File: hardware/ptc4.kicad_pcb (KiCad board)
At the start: 4 copper layers, 100 x 85 mm, 128 parts, among them J101 TNG-Power-TOP, J102 TNG-Power-BTM, J103 TNG-Data-TOP, J104 TNG-Data-BTM, P102 Debug, P103 PE, P201 INPUT0, P202 INPUT1, P203 INPUT2, P204 INPUT3, SW101 BOOT, U101 STM32F070CBT6, U102 AZ1117EH, U103 82400152, U104 TPS22975, U105 PDME1-S5-S5-S, U201 MAX31865, U202 MAX31865, U203 MAX31865, U204 MAX31865, U205 ISO7741DWR, U206 ISO7741DWR, U207 AZ1117EH, X101 TBD

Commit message: rename
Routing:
- net Net-(C120-Pad1): track 23.1 -> 34.7 mm
- net A5V: track 14.8 -> 21.6 mm
- net AGND: track 53.9 -> 60.6 mm
- net Net-(C121-Pad1): track 12.3 -> 18.4 mm
- net GND: track 170.8 -> 176.0 mm

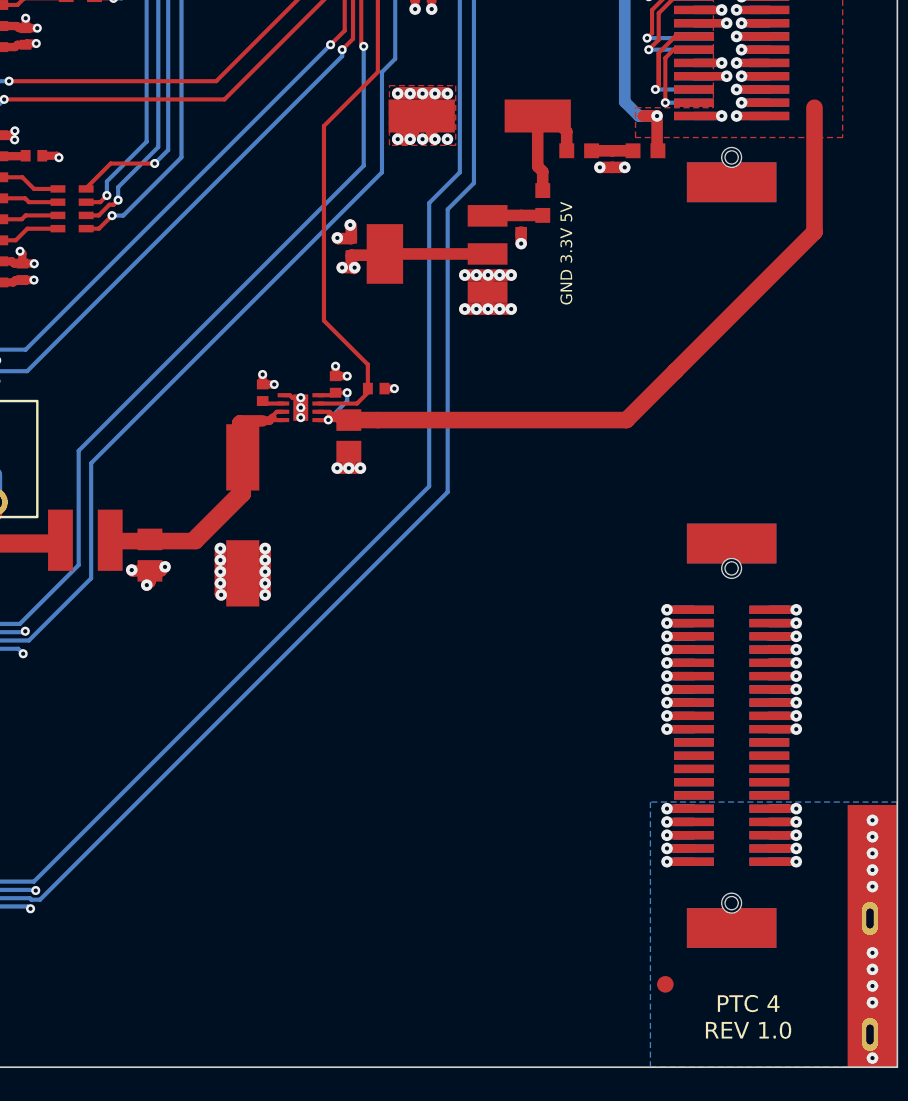
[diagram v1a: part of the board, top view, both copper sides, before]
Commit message: add version 1.1
fix footprints
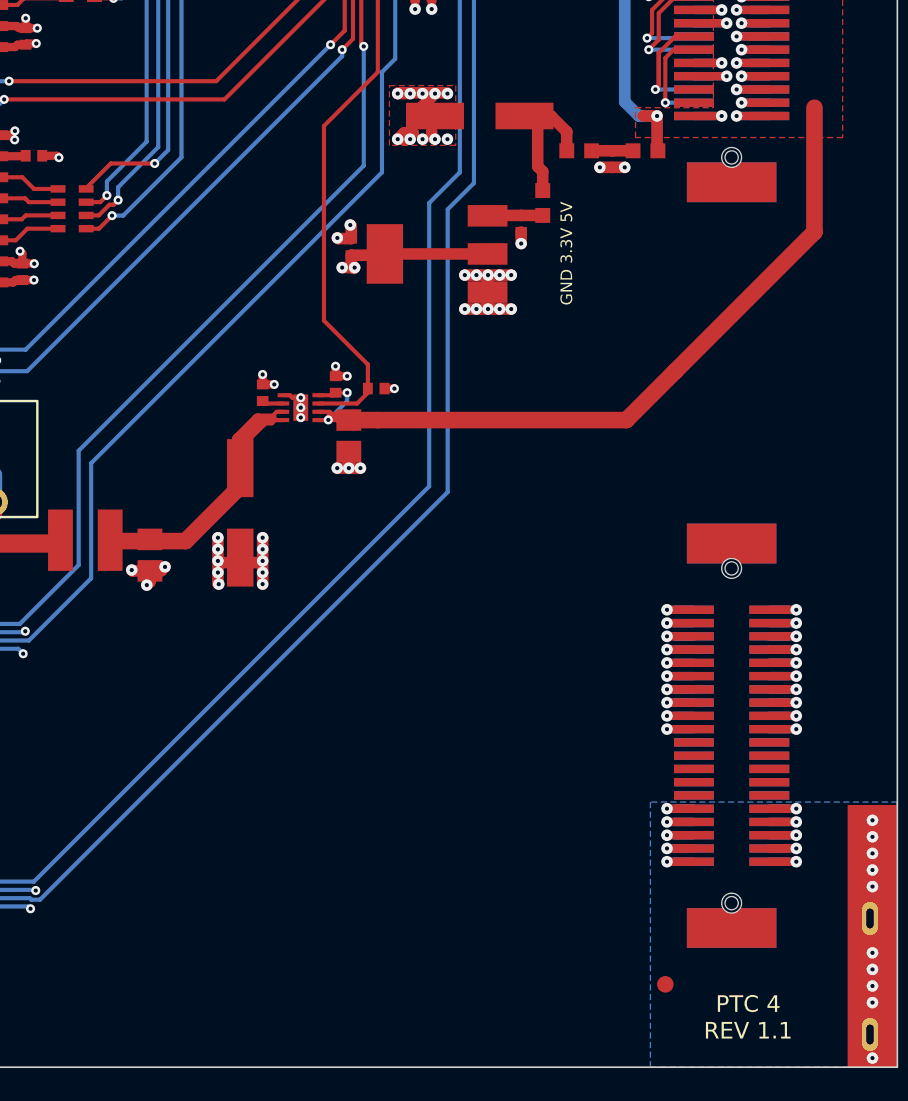
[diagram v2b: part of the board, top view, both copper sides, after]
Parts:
- C108, C109: value TBD -> 12pF
- C111, C120: value TBD -> 100µF; footprint kicad-libraries:ELKO_83 -> kicad-libraries:ELKO_63
- X101: value TBD -> 8MHz
- moved C120 0.21 mm to (150.2, 114.0)
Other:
- board text added: "Copyright Tinkerforge GmbH 2020. This documentation describes Open Hardware and is licensed under the CERN OHL v. 1.1. You may redistribute and modify this documentation under the terms of the CERN OHL v.1.1. (http://ohwr.org/cernohl). This documentation is distributed WITHOUT ANY EXPRESS OR IMPLIED WARRANTY, INCLUDING OF MERCHANTABILITY, SATISFACTORY QUALITY AND FITNESS FOR A PARTICULAR PURPOSE.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"
- board text added: "PTC 4 REV 1.1"
- board text removed: "PTC 4 REV 1.0"

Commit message: fix values
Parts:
- C108, C109: value 12pF -> 33pF
- C113, C114: value TBD/47pF -> 47pF

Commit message: fix footprint
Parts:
- C110: footprint C0805 -> kicad-libraries:C0805E

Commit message: fix values
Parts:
- C111, C120: value 100µF -> 100uF
- C121, C122, C123, C126: value 4.7µF/16V -> 4.7uF/16V
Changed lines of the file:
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@@
       (effects (font (size 0.2 0.2) (thickness 0.05)))
     )
-    (fp_text value 4.7µF/16V (at 0 -0.4) (layer F.Fab)
+    (fp_text value 4.7uF/16V (at 0 -0.4) (layer F.Fab)
       (effects (font (size 0.2 0.2) (thickness 0.05)))
     )
@@
       (effects (font (size 0.2 0.2) (thickness 0.05)))
     )
-    (fp_text value 4.7µF/16V (at 0 -0.4) (layer F.Fab)
+    (fp_text value 4.7uF/16V (at 0 -0.4) (layer F.Fab)
       (effects (font (size 0.2 0.2) (thickness 0.05)))
     )
@@
       (effects (font (size 0.2 0.2) (thickness 0.05)))
     )
-    (fp_text value 4.7µF/16V (at 0 -0.4 90) (layer F.Fab)
+    (fp_text value 4.7uF/16V (at 0 -0.4 90) (layer F.Fab)
       (effects (font (size 0.2 0.2) (thickness 0.05)))
     )
@@
       (effects (font (size 0.2 0.2) (thickness 0.05)))
     )
-    (fp_text value 4.7µF/16V (at 0 -0.4 90) (layer F.Fab)
+    (fp_text value 4.7uF/16V (at 0 -0.4 90) (layer F.Fab)
       (effects (font (size 0.2 0.2) (thickness 0.05)))
     )
@@
       (effects (font (size 0.59944 0.59944) (thickness 0.12446)))
     )
-    (fp_text value 100µF (at 0.95 -0.375) (layer F.Fab)
+    (fp_text value 100uF (at 0.95 -0.375) (layer F.Fab)
       (effects (font (size 0.59944 0.59944) (thickness 0.12446)))
     )
@@
       (effects (font (size 0.59944 0.59944) (thickness 0.12446)))
     )
-    (fp_text value 100µF (at 0.95 -0.375 90) (layer F.Fab)
+    (fp_text value 100uF (at 0.95 -0.375 90) (layer F.Fab)
       (effects (font (size 0.59944 0.59944) (thickness 0.12446)))
     )

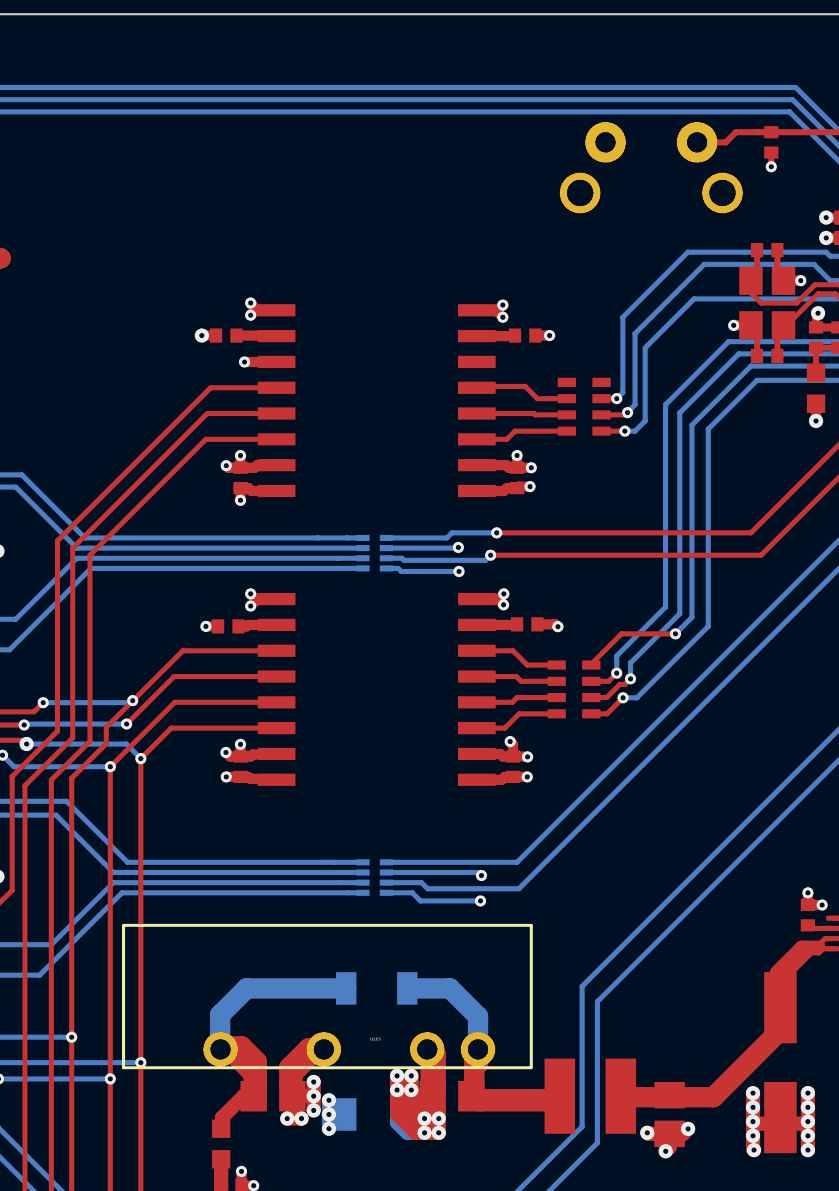
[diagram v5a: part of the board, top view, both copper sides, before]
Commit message: all footprints updated
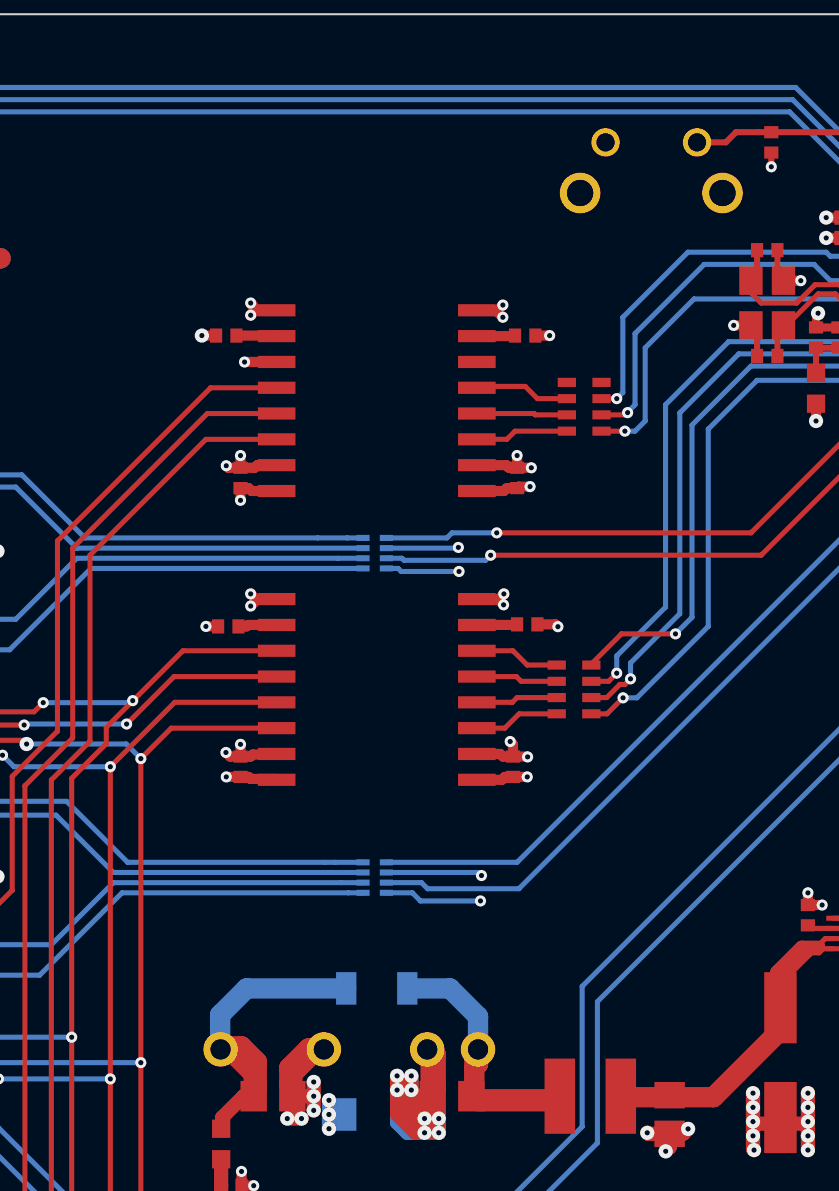
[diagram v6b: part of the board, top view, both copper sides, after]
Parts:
- C101, C102, C103, C104, C105, C106, C107, C108, C109, C112, C113, C114, C116, C117, C118, C119, C201, C202, C203, C204, C205, C206, C207, C208, C209, C210, C211, C212, C213, C214, C215, C216, C217, C218, C219: footprint C0402F -> kicad-libraries:C0402F
- C115: footprint C0603F -> kicad-libraries:C0603F
- D203, D204, D205, D206, D207, D208, D209, D210: footprint LED-LP -> kicad-libraries:LED-LP
- J101, J103: footprint TNG-40-TOP -> kicad-libraries:TNG-40-TOP
- J102, J104: footprint TNG-40-BTM -> kicad-libraries:TNG-40-BTM
- L101, L102, L103, L104, L209: footprint R0603F -> kicad-libraries:R0603F
- L105: footprint WE-CNSW-0603 -> kicad-libraries:WE-CNSW-0603
- LED101: footprint LED-RGB-LP -> kicad-libraries:LED-RGB-LP
- P201, P202, P203, P204: footprint OQ_4P -> kicad-libraries:OQ_4P
- R101, R102, R103, R104, R105, R106, R107, R108, R109: footprint R0402F -> kicad-libraries:R0402F
- U103: footprint SOT563-SPEC -> kicad-libraries:SOT563-SPEC

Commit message: default is non isolated
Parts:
- C101, C102, C103, C104, C105, C106, C107, C108, C109, C112, C113, C114, C116, C117, C118, C119, C201, C202, C203, C204, C205, C206, C207, C208, C209, C210, C211, C212, C213, C214, C215, C216, C217, C218, C219: footprint kicad-libraries:C0402F -> C0402F
- C115: footprint kicad-libraries:C0603F -> C0603F
- D203, D204, D205, D206, D207, D208, D209, D210: footprint kicad-libraries:LED-LP -> LED-LP
- J101, J103: footprint kicad-libraries:TNG-40-TOP -> TNG-40-TOP
- J102, J104: footprint kicad-libraries:TNG-40-BTM -> TNG-40-BTM
- L101, L102, L103, L104, L209: footprint kicad-libraries:R0603F -> R0603F
- L105: footprint kicad-libraries:WE-CNSW-0603 -> WE-CNSW-0603
- LED101: footprint kicad-libraries:LED-RGB-LP -> LED-RGB-LP
- P201, P202, P203, P204: footprint kicad-libraries:OQ_4P -> OQ_4P
- R101, R102, R103, R104, R105, R106, R107, R108, R109: footprint kicad-libraries:R0402F -> R0402F
- R110, R111: value DNP -> 0
- U103: footprint kicad-libraries:SOT563-SPEC -> SOT563-SPEC
- U105: value PDME1-S5-S5-S -> DNP

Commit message: fix 3d stuff
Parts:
- C101, C102, C103, C104, C105, C106, C107, C108, C109, C112, C113, C114, C116, C117, C118, C119, C201, C202, C203, C204, C205, C206, C207, C208, C209, C210, C211, C212, C213, C214, C215, C216, C217, C218, C219: footprint C0402F -> kicad-libraries:C0402F
- C115: footprint C0603F -> kicad-libraries:C0603F
- D203, D204, D205, D206, D207, D208, D209, D210: footprint LED-LP -> kicad-libraries:LED-LP
- J101, J103: footprint TNG-40-TOP -> kicad-libraries:TNG-40-TOP
- J102, J104: footprint TNG-40-BTM -> kicad-libraries:TNG-40-BTM
- L101, L102, L103, L104, L209: footprint R0603F -> kicad-libraries:R0603F
- L105: footprint WE-CNSW-0603 -> kicad-libraries:WE-CNSW-0603
- LED101: footprint LED-RGB-LP -> kicad-libraries:LED-RGB-LP
- P201, P202, P203, P204: footprint OQ_4P -> kicad-libraries:OQ_4P
- R101, R102, R103, R104, R105, R106, R107, R108, R109: footprint R0402F -> kicad-libraries:R0402F
- U103: footprint SOT563-SPEC -> kicad-libraries:SOT563-SPEC
